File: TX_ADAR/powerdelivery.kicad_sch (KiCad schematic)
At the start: 16 parts, among them IC1 REG1117A-1.8, IC2 REG1117A-2.5, SW10 SW_SPDT, SW11 SW_SPDT, SW2 SW_SPDT, SW9 SW_SPDT

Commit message: Got footprints to work
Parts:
- IC2: footprint REG1117A_1_8:SOT230P700X180-4N -> REG1117A_2_5:SOT230P700X180-4N
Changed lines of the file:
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@@
 			)
 		)
-		(property "Footprint" "REG1117A_1_8:SOT230P700X180-4N"
+		(property "Footprint" "REG1117A_2_5:SOT230P700X180-4N"
 			(at 139.7 59.69 0)
 			(hide yes)

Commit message: Finished up adding footprints. Removed unnecessary switches for the TxRST and MRST
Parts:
- C1, C2, C3, C4: footprint (none) -> Capacitor_SMD:C_0603_1608Metric_Pad1.08x0.95mm_HandSolder
- SW10, SW11, SW2, SW9: footprint (none) -> 100SP1T1B4M2QE:SW_100SP1T1B4M2QE
- TP1, TP2, TP3, TP4, TP5, TP6: footprint (none) -> TestPoint:TestPoint_Loop_D2.50mm_Drill1.0mm
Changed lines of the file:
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@@
 			)
 		)
-		(property "Footprint" ""
+		(property "Footprint" "100SP1T1B4M2QE:SW_100SP1T1B4M2QE"
 			(at 177.8 57.15 0)
 			(hide yes)
@@
 			)
 		)
-		(property "Footprint" ""
+		(property "Footprint" "100SP1T1B4M2QE:SW_100SP1T1B4M2QE"
 			(at 179.07 26.67 0)
 			(hide yes)
@@
 			)
 		)
-		(property "Footprint" ""
+		(property "Footprint" "Capacitor_SMD:C_0603_1608Metric_Pad1.08x0.95mm_HandSolder"
 			(at 117.8052 34.29 0)
 			(hide yes)
@@
 			)
 		)
-		(property "Footprint" ""
+		(property "Footprint" "Capacitor_SMD:C_0603_1608Metric_Pad1.08x0.95mm_HandSolder"
 			(at 163.5252 34.29 0)
 			(hide yes)
@@
 			)
 		)
-		(property "Footprint" ""
+		(property "Footprint" "TestPoint:TestPoint_Loop_D2.50mm_Drill1.0mm"
 			(at 167.64 26.67 0)
 			(hide yes)
@@
 			)
 		)
-		(property "Footprint" ""
+		(property "Footprint" "Capacitor_SMD:C_0603_1608Metric_Pad1.08x0.95mm_HandSolder"
 			(at 163.5252 64.77 0)
 			(hide yes)
@@
 			)
 		)
-		(property "Footprint" ""
+		(property "Footprint" "Capacitor_SMD:C_0603_1608Metric_Pad1.08x0.95mm_HandSolder"
 			(at 117.8052 64.77 0)
 			(hide yes)
@@
 			)
 		)
-		(property "Footprint" ""
+		(property "Footprint" "TestPoint:TestPoint_Loop_D2.50mm_Drill1.0mm"
 			(at 99.06 62.23 0)
 			(hide yes)
@@
 			)
 		)
-		(property "Footprint" ""
+		(property "Footprint" "100SP1T1B4M2QE:SW_100SP1T1B4M2QE"
 			(at 95.25 29.21 0)
 			(hide yes)
@@
 			)
 		)
-		(property "Footprint" ""
+		(property "Footprint" "TestPoint:TestPoint_Loop_D2.50mm_Drill1.0mm"
 			(at 186.69 29.21 0)
 			(hide yes)
@@
 			)
 		)
-		(property "Footprint" ""
+		(property "Footprint" "100SP1T1B4M2QE:SW_100SP1T1B4M2QE"
 			(at 96.52 59.69 0)
 			(hide yes)
@@
 			)
 		)
-		(property "Footprint" ""
+		(property "Footprint" "TestPoint:TestPoint_Loop_D2.50mm_Drill1.0mm"
 			(at 99.06 31.75 0)
 			(hide yes)
@@
 			)
 		)
-		(property "Footprint" ""
+		(property "Footprint" "TestPoint:TestPoint_Loop_D2.50mm_Drill1.0mm"
 			(at 167.64 57.15 0)
 			(hide yes)
@@
 			)
 		)
-		(property "Footprint" ""
+		(property "Footprint" "TestPoint:TestPoint_Loop_D2.50mm_Drill1.0mm"
 			(at 185.42 59.69 0)
 			(hide yes)

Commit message: Adding to layout
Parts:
- removed SW10, SW11: SW_SPDT, 100SP1T1B4M2QE:SW_100SP1T1B4M2QE, symbol Switch:SW_SPDT
- removed TP1, TP2, TP5, TP6: TestPoint, TestPoint:TestPoint_Loop_D2.50mm_Drill1.0mm, symbol Connector:TestPoint
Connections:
- net +5V: now also C2.1, C3.1, IC1.3 (VIN), IC2.3 (VIN)

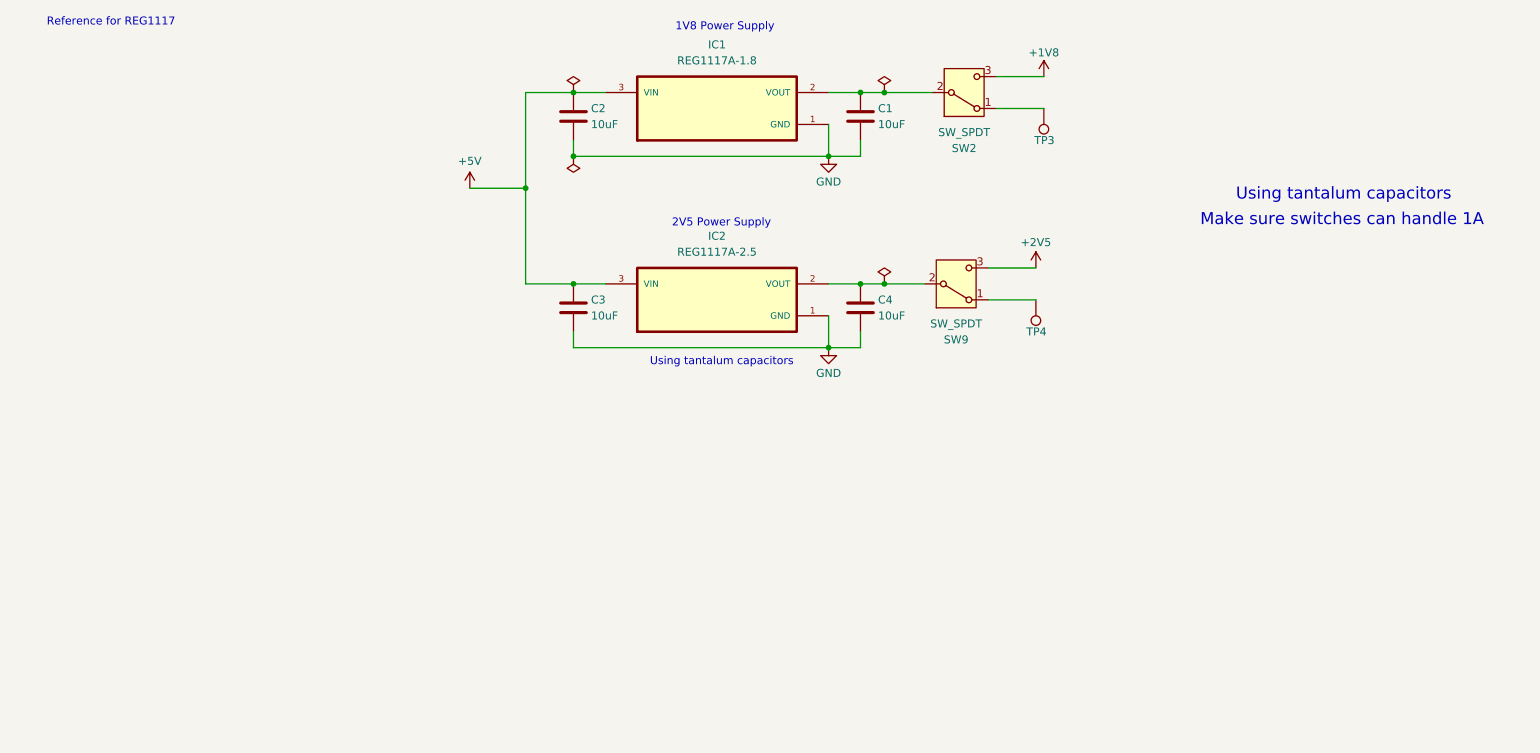
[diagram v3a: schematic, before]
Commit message: Added Level Shifters
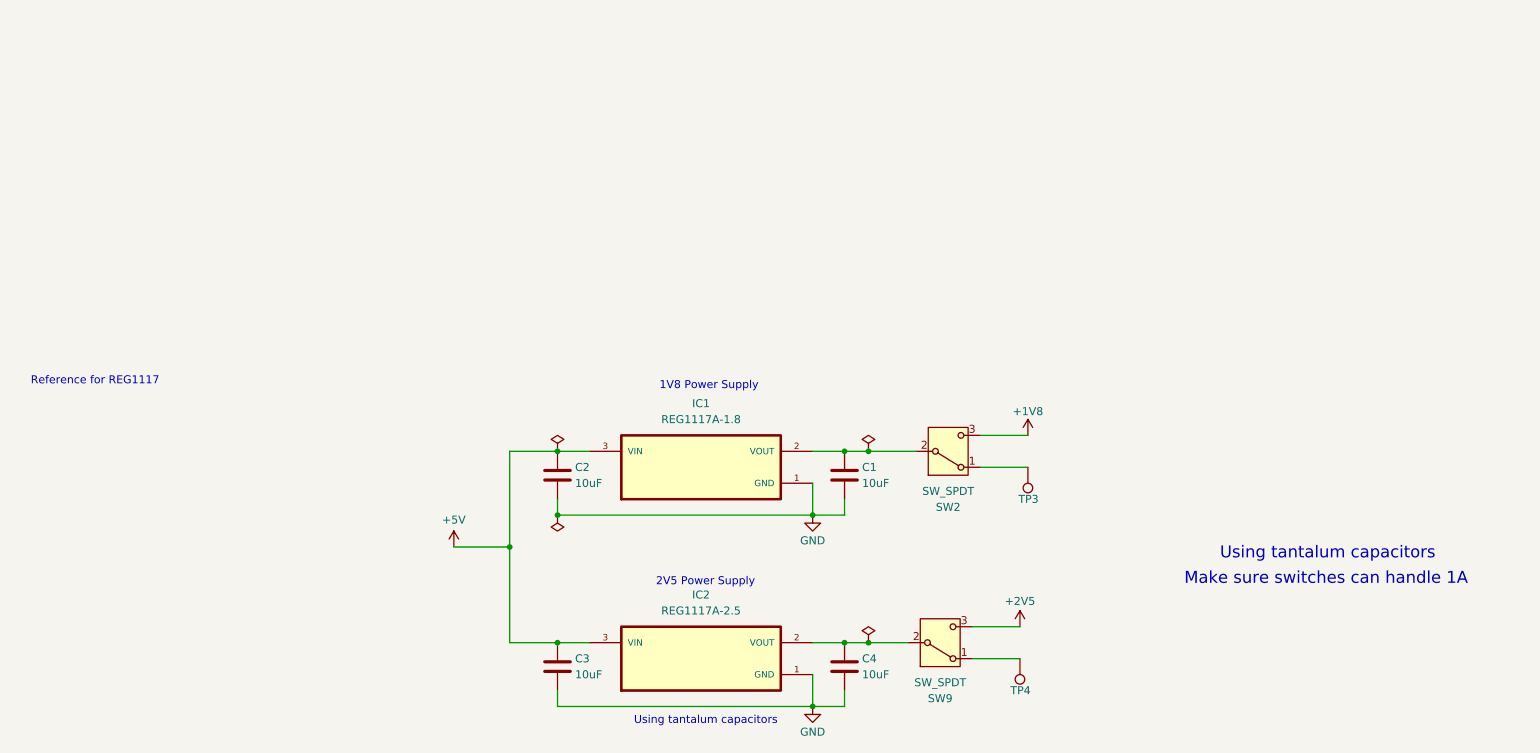
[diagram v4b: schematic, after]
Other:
- moved on the sheet: C1, C2, C3, C4, IC1, IC2, SW2, SW9, TP3, TP4
